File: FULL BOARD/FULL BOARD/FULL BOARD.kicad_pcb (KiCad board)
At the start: 2 copper layers, 200 x 200 mm, 101 parts, among them IC1 TAS5760LDAP, J1 PJ-036AH-SMT-TR, J2 Micro_SD_Card, J3 B2B-PH-K-S, J4 5019514000, J5 61201021621, J6 B2B-PH-K-S, SW1 PTS645SK50SMTR92LFS, U1 LD1117S33TR_SOT223, U2 STM32H743VITx, Y1 ABLS7M2-16.000MHZ-D-2Y-T

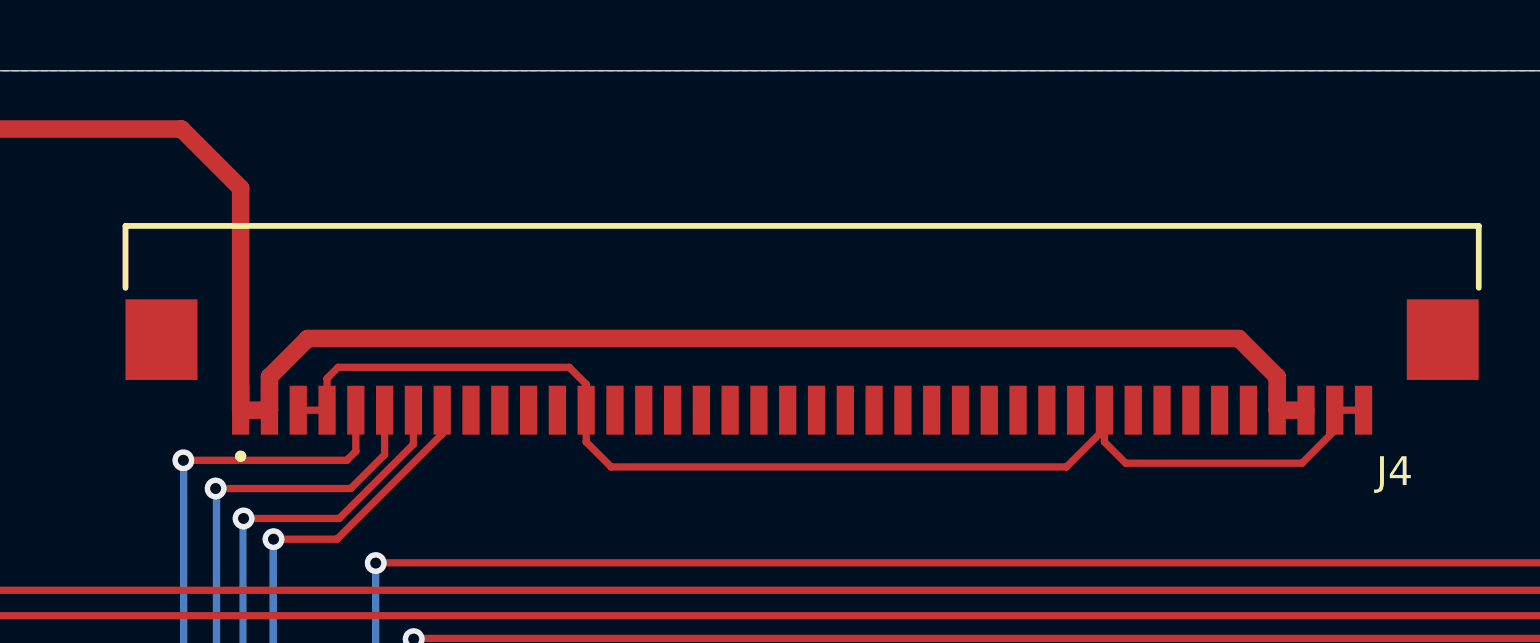
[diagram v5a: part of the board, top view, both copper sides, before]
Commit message: changed ribbon pins
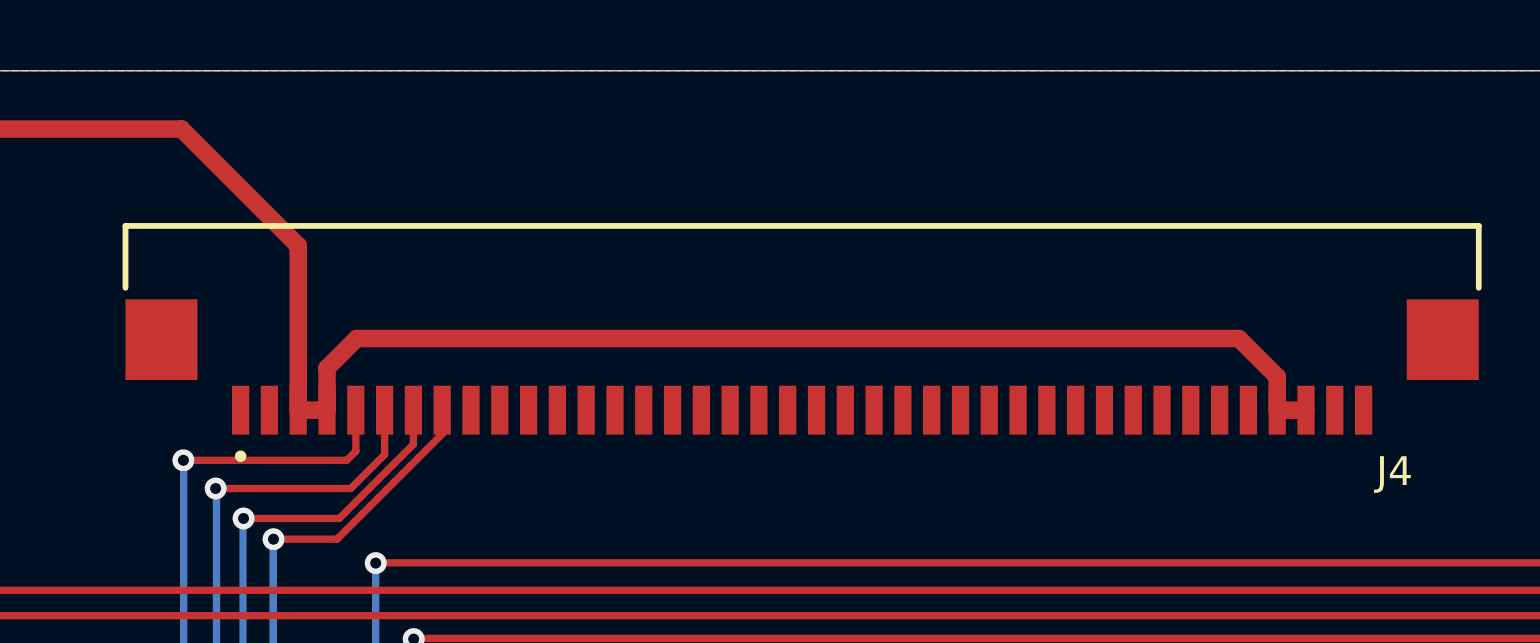
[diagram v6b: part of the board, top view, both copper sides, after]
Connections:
- J4 pad 1: +5V -> GND
- J4 pad 2: +5V -> GND
- J4 pad 3: GND -> +5V
- J4 pad 4: GND -> +5V
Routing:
- net GND: track 165.5 -> 120.8 mm
- net +5V: track 300.9 -> 299.9 mm
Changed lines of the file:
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@@
 		(at 202.0094 53.0998 180)
 		(property "Reference" "J4"
-			(at -20.575 -4.585 360)
+			(at -20.575 -4.585 0)
 			(layer "F.SilkS")
 			(effects
@@
 		)
 		(property "Value" "5019514000"
-			(at -13.59 5.165 360)
+			(at -13.59 5.165 0)
 			(layer "F.Fab")
 			(effects
@@
 		)
 		(property "Footprint" "Final Ribbon Connector:GCT_FFC3B07-40-T"
-			(at 0 0 360)
+			(at 0 0 0)
 			(layer "F.Fab")
 			(hide yes)
@@
 		)
 		(property "Datasheet" "5019514000"
-			(at 0 0 360)
+			(at 0 0 0)
 			(layer "F.Fab")
 			(hide yes)
@@
 		)
 		(property "Description" ""
-			(at 0 0 360)
+			(at 0 0 0)
 			(layer "F.Fab")
 			(hide yes)
@@
 			(size 0.6 1.7)
 			(layers "F.Cu" "F.Paste" "F.Mask")
-			(net 4 "+5V")
+			(net 2 "GND")
 			(pinfunction "1")
 			(pintype "passive")
@@
 			(size 0.6 1.7)
 			(layers "F.Cu" "F.Paste" "F.Mask")
-			(net 4 "+5V")
+			(net 2 "GND")
 			(pinfunction "2")
 			(pintype "passive")
@@
 			(size 0.6 1.7)
 			(layers "F.Cu" "F.Paste" "F.Mask")
-			(net 2 "GND")
+			(net 4 "+5V")
 			(pinfunction "3")
 			(pintype "passive")
@@
 			(size 0.6 1.7)
 			(layers "F.Cu" "F.Paste" "F.Mask")
-			(net 2 "GND")
+			(net 4 "+5V")
 			(pinfunction "4")
 			(pintype "passive")
@@
 		(tags "capacitor")
 		(property "Reference" "C18"
-			(at 0 1.68 360)
+			(at 0 1.68 0)
 			(layer "B.SilkS")
 			(effects
@@
 		)
 		(property "Value" "10nF"
-			(at 0 -1.68 360)
+			(at 0 -1.68 0)
 			(layer "B.Fab")
 			(effects
@@
 		)
 		(fp_text user "${REFERENCE}"
-			(at 0 0 360)
+			(at 0 0 0)
 			(layer "B.Fab")
 			(effects
@@
 	)
 	(segment
-		(start 195.3756 57.52)
-		(end 211.19 57.52)
-		(width 0.254)
-		(layer "F.Cu")
-		(net 2)
-	)
-	(segment
-		(start 193.92 54.06)
-		(end 194.5094 54.6494)
-		(width 0.254)
-		(layer "F.Cu")
-		(net 2)
-	)
-	(segment
 		(start 91.63 128.12)
 		(end 95.0622 128.12)
@@
 	)
 	(segment
-		(start 220.5094 56.2506)
-		(end 220.5094 55.5498)
-		(width 0.254)
-		(layer "F.Cu")
-		(net 2)
-	)
-	(segment
 		(start 82.01 137.834998)
 		(end 83.063999 137.834998)
@@
 	)
 	(segment
-		(start 212.5094 56.2006)
-		(end 212.5094 55.5498)
-		(width 0.254)
-		(layer "F.Cu")
-		(net 2)
-	)
-	(segment
 		(start 80.6504 69.1896)
 		(end 80.2438 69.5962)
@@
 	)
 	(segment
-		(start 212.5094 55.5498)
-		(end 212.5094 56.6538)
-		(width 0.254)
-		(layer "F.Cu")
-		(net 2)
-	)
-	(segment
-		(start 213.2456 57.39)
-		(end 219.37 57.39)
-		(width 0.254)
-		(layer "F.Cu")
-		(net 2)
-	)
-	(segment
 		(start 167.222592 112.001)
 		(end 166.352 112.001)
@@
 	)
 	(segment
-		(start 184.5094 55.5498)
-		(end 185.5094 55.5498)
-		(width 0.254)
-		(layer "F.Cu")
-		(net 2)
-	)
-	(segment
 		(start 84.294202 135.244998)
 		(end 84.558264 134.980936)
@@
 	)
 	(segment
-		(start 194.5094 56.6538)
-		(end 195.3756 57.52)
-		(width 0.254)
-		(layer "F.Cu")
-		(net 2)
-	)
-	(segment
 		(start 179.527 112.457)
 		(end 179.527 114.176)
@@
 	)
 	(segment
-		(start 211.19 57.52)
-		(end 212.5094 56.2006)
-		(width 0.254)
-		(layer "F.Cu")
-		(net 2)
-	)
-	(segment
 		(start 179.527 115.517)
 		(end 180.39 116.38)
@@
 	)
 	(segment
-		(start 185.8952 54.06)
-		(end 193.92 54.06)
-		(width 0.254)
-		(layer "F.Cu")
-		(net 2)
-	)
-	(segment
 		(start 83.063999 129.385)
 		(end 84.78075 131.101751)
@@
 	)
 	(segment
-		(start 194.5094 55.5498)
-		(end 194.5094 56.6538)
-		(width 0.254)
-		(layer "F.Cu")
-		(net 2)
-	)
-	(segment
 		(start 179.9336 101.0158)
 		(end 180.027 100.9224)
@@
 	)
 	(segment
-		(start 194.5094 54.6494)
-		(end 194.5094 55.5498)
-		(width 0.254)
-		(layer "F.Cu")
-		(net 2)
-	)
-	(segment
 		(start 180.027 100.9224)
 		(end 180.027 98.826)
@@
 	)
 	(segment
-		(start 221.5094 55.5498)
-		(end 220.5094 55.5498)
-		(width 0.254)
-		(layer "F.Cu")
-		(net 2)
-	)
-	(segment
 		(start 184.378 111.194)
 		(end 184.394 111.21)
@@
 	)
 	(segment
-		(start 212.5094 56.6538)
-		(end 213.2456 57.39)
-		(width 0.254)
-		(layer "F.Cu")
-		(net 2)
-	)
-	(segment
-		(start 185.5094 54.4458)
-		(end 185.8952 54.06)
-		(width 0.254)
-		(layer "F.Cu")
-		(net 2)
-	)
-	(segment
 		(start 91.62 128.13)
 		(end 91.63 128.12)
@@
 	)
 	(segment
-		(start 185.5094 55.5498)
-		(end 185.5094 54.4458)
-		(width 0.254)
-		(layer "F.Cu")
-		(net 2)
-	)
-	(segment
 		(start 85.91 128.21)
 		(end 85.91 132.013)
@@
 	)
 	(segment
-		(start 219.37 57.39)
-		(end 220.5094 56.2506)
-		(width 0.254)
-		(layer "F.Cu")
-		(net 2)
-	)
-	(segment
 		(start 176.25 111.312003)
 		(end 178.382003 111.312003)
@@
 	)
 	(segment
-		(start 182.5094 47.8386)
-		(end 182.5094 55.5498)
+		(start 104.3284 52.24)
+		(end 104.3284 47.17)
 		(width 0.6096)
 		(layer "F.Cu")
@@
 	)
 	(segment
-		(start 104.3284 47.17)
-		(end 105.7134 45.785)
+		(start 105.7134 45.785)
+		(end 180.4558 45.785)
 		(width 0.6096)
 		(layer "F.Cu")
@@
 	(segment
 		(start 89.5442 59.25371)
+		(end 97.31469 59.25371)
+		(width 0.6096)
+		(layer "F.Cu")
+		(net 4)
+	)
+	(segment
+		(start 89.5442 59.25371)
 		(end 85.3492 63.44871)
 		(width 0.6096)
@@
 	)
 	(segment
-		(start 183.5094 54.3902)
-		(end 184.839 53.0606)
-		(width 0.6096)
-		(layer "F.Cu")
-		(net 4)
-	)
-	(segment
-		(start 180.4558 45.785)
-		(end 182.5094 47.8386)
-		(width 0.6096)
-		(layer "F.Cu")
-		(net 4)
-	)
-	(segment
 		(start 87.163 75.0608)
 		(end 87.291 75.1888)
@@
 	)
 	(segment
-		(start 184.839 53.0606)
-		(end 217.1798 53.0606)
-		(width 0.6096)
-		(layer "F.Cu")
-		(net 4)
-	)
-	(segment
 		(start 74.12 126.05)
 		(end 74.12 131.3004)
@@
 	)
 	(segment
-		(start 89.5442 59.25371)
-		(end 97.31469 59.25371)
-		(width 0.6096)
-		(layer "F.Cu")
-		(net 4)
-	)
-	(segment
 		(start 87.291 69.7014)
 		(end 87.291 75.1888)
@@
 	)
 	(segment
-		(start 80.255002 131.344998)
-		(end 82.0192 131.344998)
-		(width 0.254)
+		(start 97.31469 59.25371)
+		(end 104.3284 52.24)
+		(width 0.6096)
 		(layer "F.Cu")
 		(net 4)
 	)
 	(segment
-		(start 183.5094 55.5498)
-		(end 183.5094 54.3902)
-		(width 0.6096)
+		(start 80.255002 131.344998)
+		(end 82.0192 131.344998)
+		(width 0.254)
 		(layer "F.Cu")
 		(net 4)
@@
 	)
 	(segment
-		(start 104.3284 52.24)
-		(end 104.3284 47.17)
+		(start 184.5094 55.5498)
+		(end 185.5094 55.5498)
+		(width 0.6096)
+		(layer "F.Cu")
+		(net 4)
+	)
+	(segment
+		(start 180.4558 45.785)
+		(end 184.5094 49.8386)
 		(width 0.6096)
 		(layer "F.Cu")
@@
 	)
 	(segment
-		(start 97.31469 59.25371)
-		(end 104.3284 52.24)
+		(start 185.5094 54.0902)
+		(end 186.539 53.0606)
 		(width 0.6096)
 		(layer "F.Cu")
@@
 	)
 	(segment
-		(start 105.7134 45.785)
-		(end 180.4558 45.785)
-		(width 0.6096)
+		(start 79.6 132)
+		(end 80.255002 131.344998)
+		(width 0.254)
 		(layer "F.Cu")
 		(net 4)
 	)
 	(segment
-		(start 79.6 132)
-		(end 80.255002 131.344998)
-		(width 0.254)
+		(start 186.539 53.0606)
+		(end 217.1798 53.0606)
+		(width 0.6096)
 		(layer "F.Cu")
 		(net 4)
@@
 	)
 	(segment
-		(start 182.5094 55.5498)
-		(end 183.5094 55.5498)
+		(start 184.5094 49.8386)
+		(end 184.5094 55.5498)
+		(width 0.6096)
+		(layer "F.Cu")
+		(net 4)
+	)
+	(segment
+		(start 185.5094 55.5498)
+		(end 185.5094 54.0902)
 		(width 0.6096)
 		(layer "F.Cu")
@@
 		(layer "F.Cu")
 		(net 4)
+	)
+	(segment
+		(start 104.3284 47.17)
+		(end 105.7134 45.785)
+		(width 0.6096)
+		(layer "F.Cu")
+		(net 4)
